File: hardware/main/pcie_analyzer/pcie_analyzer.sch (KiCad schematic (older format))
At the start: 23 parts

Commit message: vunit, sch work
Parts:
- added C? (x18): 100n, symbol pcie_analyzer:C
- added C? (x8): 4.7u, symbol pcie_analyzer:C
- added C? (x12): 1n, symbol pcie_analyzer:C
- added D? (x2): HMC914, symbol pcie_analyzer:HMC914
- added R? (x4): 4.75K, symbol pcie_analyzer:R
- added R? (x2): 1.82K, symbol pcie_analyzer:R
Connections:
- net +3.3VCC: now also C?.1, C?.1, C?.1, C?.1, C?.1, C?.1, C?.1, C?.1, C?.1, C?.1, C?.1, C?.1, C?.1, C?.1, C?.1, C?.1, D?.18 (VCC), D?.18 (VCC), D?.21 (VCC), D?.21 (VCC), D?.22 (VCC), D?.22 (VCC), R?.2, R?.2
- net GND: now also C?.2, C?.2, C?.2, C?.2, C?.2, C?.2, C?.2, C?.2, C?.2, C?.2, C?.2, C?.2, C?.2, C?.2, C?.2, C?.2, C?.2, C?.2, C?.2, C?.2, C?.2, C?.2, C?.2, C?.2, C?.2, C?.2, C?.2, C?.2, C?.2, C?.2, C?.2, C?.2, C?.2, C?.2, C?.2, C?.2, D?.11 (GND), D?.11 (GND), D?.12 (GND), D?.12 (GND), D?.13 (N/C), D?.13 (N/C), D?.14 (GND), D?.14 (GND), D?.17 (GND), D?.17 (GND), D?.2 (GND), D?.2 (GND), D?.5 (GND), D?.5 (GND), D?.8 (GND), D?.8 (GND), D?.9 (GND), D?.9 (GND), D?.EP (GND), D?.EP (GND), R?.1, R?.1
- net RSSI: now also D?.23 (RSSI), D?.23 (RSSI)
- net AODWNENB renamed AODWNENB_UP
- net DISABLE renamed DISABLE_UP
- net VAC renamed VAC_UP
- new net: D?.1 (LOS), R?.1 (x2)
- new net: C?.1, D?.19 (CN) (x2)
- new net: C?.2, D?.20 (CP) (x2)
- new net: C?.1, C?.1, D?.24 (LOSTH), R?.2 (x2)
- new net: R?.1, R?.2 (x2)
- new net AODWNENB_CLK: C?.1, C?.1, C?.1, D?.7 (AODWNENB)
- new net AODWNENB_DOWN: C?.1, C?.1, C?.1, D?.7 (AODWNENB)
- new net CLK_N: D?.4 (INN)
- new net CLK_P: D?.3 (INP)
- new net DISABLE_CLK: C?.1, C?.1, C?.1, D?.6 (DISABLE)
- new net DISABLE_DOWN: C?.1, C?.1, C?.1, D?.6 (DISABLE)
- new net PCIE_2_N: D?.15 (QN)
- new net PCIE_2_P: D?.16 (QP)
- new net PCIE_CLK_N: D?.15 (QN)
- new net PCIE_CLK_P: D?.16 (QP)
- new net PCIE_DOWN_N: D?.4 (INN)
- new net PCIE_DOWN_P: D?.3 (INP)
- new net VAC_CLK: C?.1, C?.1, D?.10 (VAC)
- new net VAC_DOWN: C?.1, C?.1, D?.10 (VAC)

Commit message: schema update
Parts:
- added J? (x2): HDR40, symbol pcie_analyzer:HDR40
- added J? (x6): Conn_Coaxial, symbol pcie_analyzer:Conn_Coaxial
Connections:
- net +3.3VCC: now also J?.20, J?.25, J?.27, J?.35, J?.37, J?.39
- net GND: now also J?.1, J?.19, J?.2, J?.2 (Ext), J?.2 (Ext), J?.2 (Ext), J?.2 (Ext), J?.2 (Ext), J?.2 (Ext), J?.22, J?.22, J?.24, J?.24, J?.26, J?.26, J?.28, J?.3, J?.3, J?.3, J?.3, J?.3, J?.3, J?.30, J?.30, J?.32, J?.34, J?.34, J?.36, J?.38, J?.4, J?.4, J?.4, J?.4, J?.4, J?.4, J?.40, J?.40, J?.5, J?.5, J?.5, J?.5, J?.5, J?.5
- net PCIE_1_N: now also J?.1 (In)
- net PCIE_1_P: now also J?.1 (In)
- net PCIE_2_N: now also J?.1 (In)
- net PCIE_2_P: now also J?.1 (In)
- net PCIE_CLK_N: now also J?.1 (In)
- net PCIE_CLK_P: now also J?.1 (In)
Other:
- moved on the sheet: C?, D?, R?

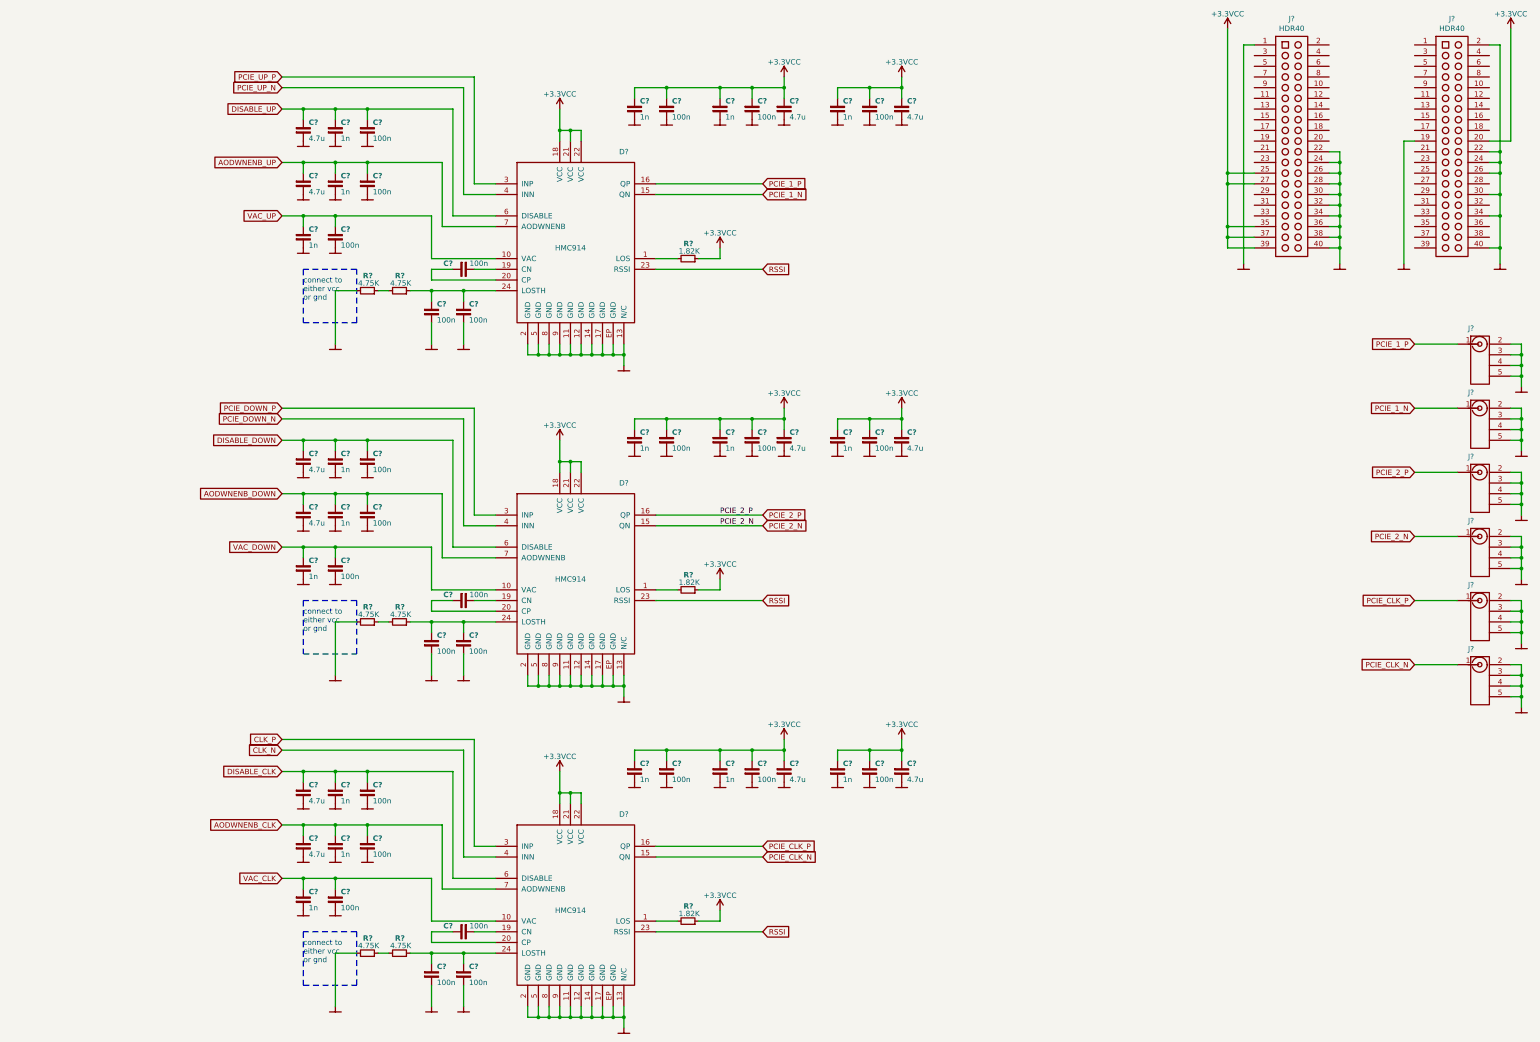
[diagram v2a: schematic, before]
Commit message: schema update, opAmp replaced with ONET1191P
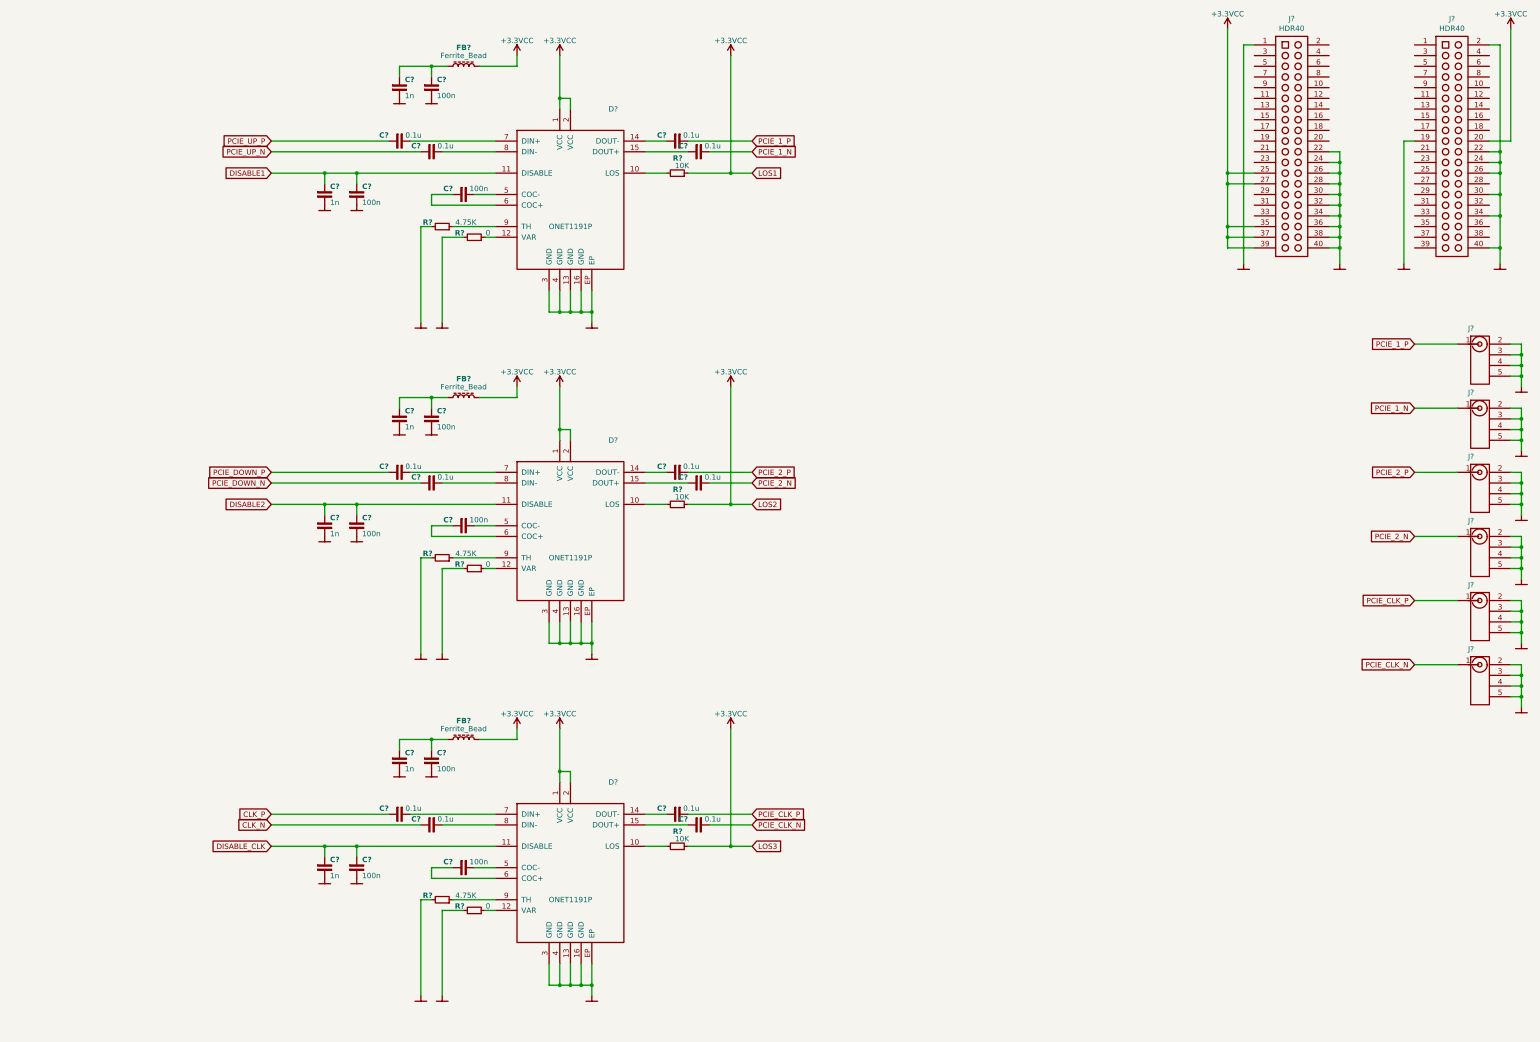
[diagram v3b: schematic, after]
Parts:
- removed C? (x24): 100n, symbol pcie_analyzer:C
- removed C? (x12): 4.7u, symbol pcie_analyzer:C
- removed C? (x16): 1n, symbol pcie_analyzer:C
- removed D? (x3): HMC914, symbol pcie_analyzer:HMC914
- removed R? (x6): 4.75K, symbol pcie_analyzer:R
- removed R? (x2): 1.82K, symbol pcie_analyzer:R
- added C? (x12): 0.1u, symbol pcie_analyzer:C
- added C? (x6): 100n, symbol pcie_analyzer:C
- added C? (x4): 1n, symbol pcie_analyzer:C
- added D? (x3): ONET1191P, symbol pcie_analyzer:ONET1191P
- added FB? (x3): Ferrite_Bead, symbol pcie_analyzer:Ferrite_Bead
- added R? (x3): 4.75K, symbol pcie_analyzer:R
- added R? (x3): 0, symbol pcie_analyzer:R
- added R? (x2): 10K, symbol pcie_analyzer:R
- R?: value 1.82K -> 10K
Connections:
- net +3.3VCC: now also D?.1 (VCC), D?.1 (VCC), D?.1 (VCC), D?.2 (VCC), D?.2 (VCC), D?.2 (VCC), FB?.2, FB?.2, FB?.2, R?.2, R?.2; no longer C?.1, C?.1
- net CLK_N: now also C?.2
- net CLK_P: now also C?.2
- net DISABLE_CLK: now also C?.1, C?.1, D?.11 (DISABLE)
- net GND: now also C?.2, C?.2, C?.2, C?.2, C?.2, C?.2, C?.2, C?.2, D?.13 (GND), D?.13 (GND), D?.13 (GND), D?.16 (GND), D?.16 (GND), D?.16 (GND), D?.3 (GND), D?.3 (GND), D?.3 (GND), D?.4 (GND), D?.4 (GND), D?.4 (GND), D?.EP, D?.EP, D?.EP, R?.1, R?.1, R?.1, R?.1, R?.1, R?.1
- net PCIE_1_N: now also C?.1
- net PCIE_1_P: now also C?.1
- net PCIE_2_N: now also C?.1
- net PCIE_2_P: now also C?.1
- net PCIE_CLK_N: now also C?.1
- net PCIE_CLK_P: now also C?.1
- net PCIE_DOWN_N: now also C?.2
- net PCIE_DOWN_P: now also C?.2
- net PCIE_UP_N: now also C?.2
- net PCIE_UP_P: now also C?.2
- net at R?.1: now also D?.10 (LOS)
- net at C?.1: now also D?.5 (COC-)
- net at C?.2: now also D?.6 (COC+)
- net DISABLE_UP renamed DISABLE1
- net DISABLE1: now also D?.11 (DISABLE)
- new net: C?.1, C?.1, FB?.1 (x3)
- new net: D?.12 (VAR), R?.2 (x3)
- new net: C?.2, D?.14 (DOUT-) (x3)
- new net: C?.2, D?.15 (DOUT+) (x3)
- new net: C?.1, D?.7 (DIN+) (x3)
- new net: C?.1, D?.8 (DIN-) (x3)
- new net: D?.9 (TH), R?.2 (x3)
- new net: C?.1, D?.5 (COC-) (x2)
- new net: C?.2, D?.6 (COC+) (x2)
- new net: D?.10 (LOS), R?.1 (x2)
- new net DISABLE2: C?.1, C?.1, D?.11 (DISABLE)
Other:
- note removed: "connect to \neither vcc\nor gnd"
- moved on the sheet: C?, R?
